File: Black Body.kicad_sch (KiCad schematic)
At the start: 20 parts, among them IC2 MCP96L00T-E_MX, J1 53307-2471, J2 Conn_01x02, J3 Conn_01x03, J4 Conn_02x08_Top_Bottom

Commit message: Revision
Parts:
- added TP1, TP2, TP3, TP4, TP5, TP6, TP7, TP8: TestPoint, Connector_PinHeader_2.54mm:PinHeader_1x01_P2.54mm_Vertical, symbol Connector:TestPoint
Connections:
- net +3V3: now also TP4.1
- net GND: now also TP5.1, TP6.1, TP7.1, TP8.1
- net at IC2.19 (SCL), J1.6 (I2C1_SCL), J3.1 (Pin_1): now also TP1.1
- net at IC2.20 (SDA), J1.4 (I2C1_SDA), J3.2 (Pin_2): now also TP2.1
- net at J1.9 (ADC1_IN7), J3.3 (Pin_3): now also TP3.1

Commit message: Updated Layout
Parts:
- removed D1, D2, D3, D4: 3V3, Diode_SMD:D_0603_1608Metric_Pad1.05x0.95mm_HandSolder, symbol Device:D
- removed J3: Conn_01x03, Connector_Molex:Molex_Nano-Fit_105313-xx03_1x03_P2.50mm_Horizontal, symbol Connector_Generic:Conn_01x03
- removed R4: 1M, Resistor_SMD:R_0603_1608Metric_Pad0.98x0.95mm_HandSolder, symbol Device:R_US
- removed R7, R8: 2M, Resistor_SMD:R_0603_1608Metric_Pad0.98x0.95mm_HandSolder, symbol Device:R_US
- removed TP7, TP8: TestPoint, Connector_PinHeader_2.54mm:PinHeader_1x01_P2.54mm_Vertical, symbol Connector:TestPoint
- added D1, D2, D3, D4, D5: LED, LED_SMD:LED_0603_1608Metric_Pad1.05x0.95mm_HandSolder, symbol Device:LED
- added J3: Conn_01x03_Pin, Connector_Molex:Molex_Nano-Fit_105313-xx03_1x03_P2.50mm_Horizontal, symbol Connector:Conn_01x03_Pin
- added J5: Conn_01x06, Connector_Molex:Molex_Nano-Fit_105313-xx06_1x06_P2.50mm_Horizontal, symbol Connector_Generic:Conn_01x06
- added R1: 10k, Resistor_SMD:R_0805_2012Metric, symbol Device:R_US
- added R10, R4, R7, R8, R9: R, Resistor_SMD:R_0603_1608Metric_Pad0.98x0.95mm_HandSolder, symbol Device:R
- added R2, R3: 1.5k, Resistor_SMD:R_0805_2012Metric, symbol Device:R_US
- added TP_TC_1, TP_TC_2, TP_TC_F_1, TP_TC_F_2: TestPoint, Connector_PinHeader_2.54mm:PinHeader_1x01_P2.54mm_Vertical, symbol Connector:TestPoint
- J4: footprint MX150:CONN_SD-75900-001_2X08_MOL -> Blackbody Footprint:CONN_SD-75900-001_2X08_MOL
- renumbered TP5 to GND1, TP6 to GND2, TP3 to INT1, TP1 to IS_SCL1, TP2 to IS_SDA1, TP4 to VCC1
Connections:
- net +3V3: now also C2.2, J5.3 (Pin_3), R1.1, R10.2, R2.1, R3.1, R4.2, R7.2, R8.2, R9.2; no longer C2.1, IC2.8 (GND_6)
- net GND: now also C2.1, IC2.8 (GND_6), J4.8 (Pin_8), J5.1 (Pin_1), J5.2 (Pin_2); no longer C2.2
- net at FB1.1, J2.1 (Pin_1): now also TP_TC_1.1
- net at C3.1, IC2.2 (VIN+), R6.1: now also TP_TC_F_2.1
- net at C3.2, IC2.4 (VIN-), R5.1: now also TP_TC_F_1.1
- net I2C1_SCL: now reaches IC2.19 (SCL), IS_SCL1.1, J1.6 (I2C1_SCL)
- net I2C1_SCL: now also D3.1 (K), J3.2 (Pin_2), J5.5 (Pin_5), R2.2
- net I2C1_SDA: now reaches IC2.20 (SDA), IS_SDA1.1, J1.4 (I2C1_SDA)
- net I2C1_SDA: now also J3.1 (Pin_1), J5.4 (Pin_4), R3.2
- net INT: now reaches INT1.1, J1.9 (ADC1_IN7)
- net INT: now also J3.3 (Pin_3), J5.6 (Pin_6), R1.2
- net at FB2.1, J2.2 (Pin_2): now also TP_TC_2.1
- net Alert_1: now reaches IC2.11 (ALERT_1)
- net Alert_1: now also J1.12 (SPI2_NSS)
- net Alert_2: now reaches IC2.12 (ALERT_2)
- net Alert_2: now also J1.18 (SPI2_SCK)
- net Alert_3: now reaches IC2.14 (ALERT_3)
- net Alert_3: now also J1.16 (SPI2_MOSI)
- net Alert_4: now reaches IC2.15 (ALERT_4)
- net Alert_4: now also J1.14 (SPI2_MISO)
- net DB_Conn_2: now reaches J1.17 (SPI1_MOSI)
- net DB_Conn_2: now also D4.1 (K)
- net Heartbeat: now reaches J1.19 (SPI1_NSS)
- net Heartbeat: now also D2.1 (K)
- net CAN_L: now reaches J1.20 (CAN_L), J4.6 (Pin_6)
- net CAN_L: now also J4.12 (Pin_12)
- net DB_Conn_3: now reaches J1.21 (SPI1_MISO)
- net DB_Conn_3: now also D5.1 (K)
- net CAN_H: now reaches J1.22 (CAN_H), J4.5 (Pin_5)
- net CAN_H: now also J4.13 (Pin_13)
- net DB_Conn_1: now reaches J1.23 (SPI1_SCK)
- net DB_Conn_1: now also D1.1 (K)
- net +24V: now reaches J1.24 (+24V_In), J4.1 (Pin_1)
- net +24V: now also J4.9 (Pin_9)
- new net: D1.2 (A), R4.1
- new net: D2.2 (A), R8.1
- new net: D4.2 (A), R7.1
- new net: D5.2 (A), R10.1
- new net: D3.2 (A), R9.1
- no-connect marks 34 -> 18
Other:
- moved on the sheet: C2, C3, FB1, FB2, GND1, GND2, IC2, INT1, IS_SCL1, IS_SDA1, J1, J2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

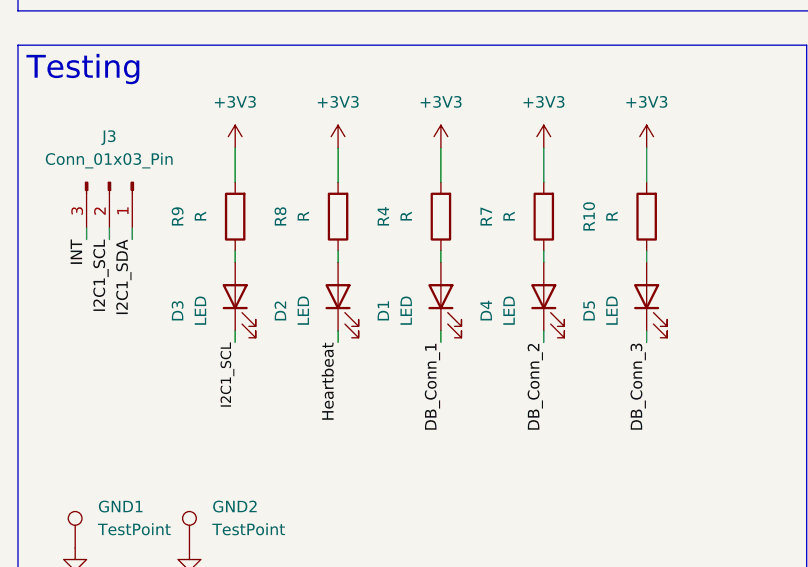
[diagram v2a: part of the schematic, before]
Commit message: resistors added
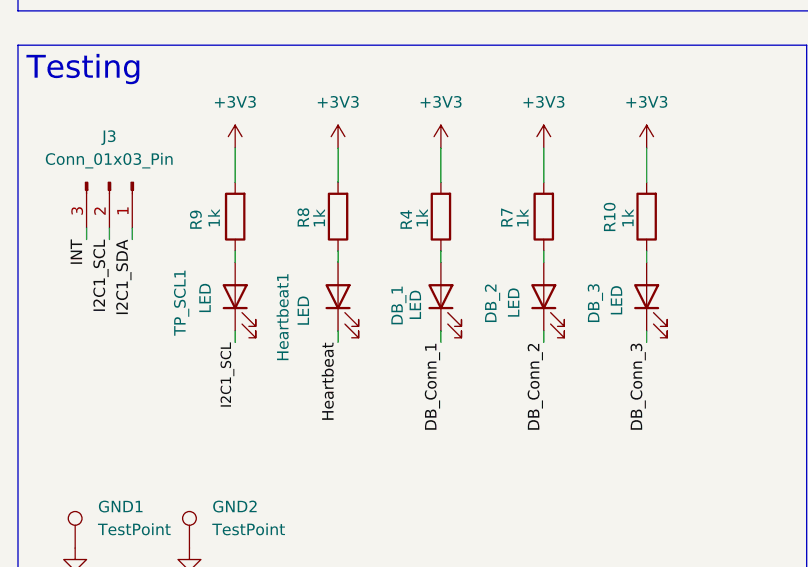
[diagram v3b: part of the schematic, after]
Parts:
- J4: footprint Blackbody Footprint:CONN_SD-75900-001_2X08_MOL -> UTSVT_Connectors:CONN_SD-75900-001_2X08_MOL
- R10, R4, R7, R8, R9: value R -> 1k
- renumbered D1 to DB_1, D4 to DB_2, D5 to DB_3, D2 to Heartbeat1, D3 to TP_SCL1
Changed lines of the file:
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@@
 		(on_board yes)
 		(dnp no)
-		(fields_autoplaced yes)
-		(property "Reference" "D1"
-			(at 57.15 138.7475 0)
+		(property "Reference" "DB_1"
+			(at 58.674 135.89 0)
 			(effects
 				(font
 					(size 1.27 1.27)
 				)
+				(justify right)
 			)
 		)
 		(property "Value" "LED"
-			(at 59.69 138.7475 0)
+			(at 60.706 136.398 0)
 			(effects
 				(font
 					(size 1.27 1.27)
 				)
+				(justify right)
 			)
 		)
@@
 			(project "Black Body"
 				(path "/326551d7-59c6-4bc5-b0df-e38f608d8925"
-					(reference "D1")
+					(reference "DB_1")
 					(unit 1)
 				)
@@
 		(on_board yes)
 		(dnp no)
-		(fields_autoplaced yes)
-		(property "Reference" "D2"
-			(at 45.72 138.7475 0)
+		(property "Reference" "Heartbeat1"
+			(at 45.974 139.446 0)
 			(effects
 				(font
@@
 			(project "Black Body"
 				(path "/326551d7-59c6-4bc5-b0df-e38f608d8925"
-					(reference "D2")
+					(reference "Heartbeat1")
 					(unit 1)
 				)
@@
 		(on_board yes)
 		(dnp no)
-		(fields_autoplaced yes)
 		(property "Reference" "R7"
-			(at 68.58 128.27 90)
+			(at 70.866 129.54 90)
 			(effects
 				(font
 					(size 1.27 1.27)
 				)
+				(justify right)
 			)
 		)
-		(property "Value" "R"
-			(at 71.12 128.27 90)
+		(property "Value" "1k"
+			(at 72.644 129.54 90)
 			(effects
 				(font
 					(size 1.27 1.27)
 				)
+				(justify right)
 			)
 		)
@@
 		(on_board yes)
 		(dnp no)
-		(fields_autoplaced yes)
-		(property "Reference" "D5"
-			(at 80.01 138.7475 0)
+		(property "Reference" "DB_3"
+			(at 80.518 135.636 0)
 			(effects
 				(font
 					(size 1.27 1.27)
 				)
+				(justify right)
 			)
 		)
 		(property "Value" "LED"
-			(at 82.55 138.7475 0)
+			(at 83.058 135.89 0)
 			(effects
 				(font
 					(size 1.27 1.27)
 				)
+				(justify right)
 			)
 		)
@@
 			(project "Black Body"
 				(path "/326551d7-59c6-4bc5-b0df-e38f608d8925"
-					(reference "D5")
+					(reference "DB_3")
 					(unit 1)
 				)
@@
 		(on_board yes)
 		(dnp no)
-		(fields_autoplaced yes)
 		(property "Reference" "R9"
-			(at 34.29 128.27 90)
+			(at 36.322 129.794 90)
 			(effects
 				(font
 					(size 1.27 1.27)
 				)
+				(justify right)
 			)
 		)
-		(property "Value" "R"
-			(at 36.83 128.27 90)
+		(property "Value" "1k"
+			(at 38.354 129.54 90)
 			(effects
 				(font
 					(size 1.27 1.27)
 				)
+				(justify right)
 			)
 		)
@@
 		(on_board yes)
 		(dnp no)
-		(fields_autoplaced yes)
-		(property "Reference" "D4"
-			(at 68.58 138.7475 0)
+		(property "Reference" "DB_2"
+			(at 69.088 135.636 0)
 			(effects
 				(font
 					(size 1.27 1.27)
 				)
+				(justify right)
 			)
 		)
 		(property "Value" "LED"
-			(at 71.12 138.7475 0)
+			(at 71.628 136.144 0)
 			(effects
 				(font
 					(size 1.27 1.27)
 				)
+				(justify right)
 			)
 		)
@@
 			(project "Black Body"
 				(path "/326551d7-59c6-4bc5-b0df-e38f608d8925"
-					(reference "D4")
+					(reference "DB_2")
 					(unit 1)
 				)
@@
 		(on_board yes)
 		(dnp no)
-		(fields_autoplaced yes)
 		(property "Reference" "R10"
-			(at 80.01 128.27 90)
+			(at 82.296 130.048 90)
 			(effects
 				(font
 					(size 1.27 1.27)
 				)
+				(justify right)
 			)
 		)
-		(property "Value" "R"
-			(at 82.55 128.27 90)
+		(property "Value" "1k"
+			(at 84.328 129.54 90)
 			(effects
 				(font
 					(size 1.27 1.27)
 				)
+				(justify right)
 			)
 		)
@@
 		(on_board yes)
 		(dnp no)
-		(fields_autoplaced yes)
 		(property "Reference" "R8"
-			(at 45.72 128.27 90)
+			(at 48.26 129.54 90)
 			(effects
 				(font
 					(size 1.27 1.27)
 				)
+				(justify right)
 			)
 		)
-		(property "Value" "R"
-			(at 48.26 128.27 90)
+		(property "Value" "1k"
+			(at 50.038 129.54 90)
 			(effects
 				(font
 					(size 1.27 1.27)
 				)
+				(justify right)
 			)
 		)
@@
 		(on_board yes)
 		(dnp no)
-		(fields_autoplaced yes)
 		(property "Reference" "R4"
-			(at 57.15 128.27 90)
+			(at 59.69 129.794 90)
 			(effects
 				(font
 					(size 1.27 1.27)
 				)
+				(justify right)
 			)
 		)
-		(property "Value" "R"
-			(at 59.69 128.27 90)
+		(property "Value" "1k"
+			(at 61.468 129.54 90)
 			(effects
 				(font
 					(size 1.27 1.27)
 				)
+				(justify right)
 			)
 		)
@@
 		(on_board yes)
 		(dnp no)
-		(fields_autoplaced yes)
-		(property "Reference" "D3"
-			(at 34.29 138.7475 0)
+		(property "Reference" "TP_SCL1"
+			(at 34.544 134.112 0)
 			(effects
 				(font
 					(size 1.27 1.27)
 				)
+				(justify right)
 			)
 		)
 		(property "Value" "LED"
-			(at 36.83 138.7475 0)
+			(at 37.338 135.636 0)
 			(effects
 				(font
 					(size 1.27 1.27)
 				)
+				(justify right)
 			)
 		)
@@
 			(project "Black Body"
 				(path "/326551d7-59c6-4bc5-b0df-e38f608d8925"
-					(reference "D3")
+					(reference "TP_SCL1")
 					(unit 1)
 				)
@@
 			)
 		)
-		(property "Footprint" "Blackbody Footprint:CONN_SD-75900-001_2X08_MOL"
+		(property "Footprint" "UTSVT_Connectors:CONN_SD-75900-001_2X08_MOL"
 			(at 135.89 132.08 0)
 			(effects

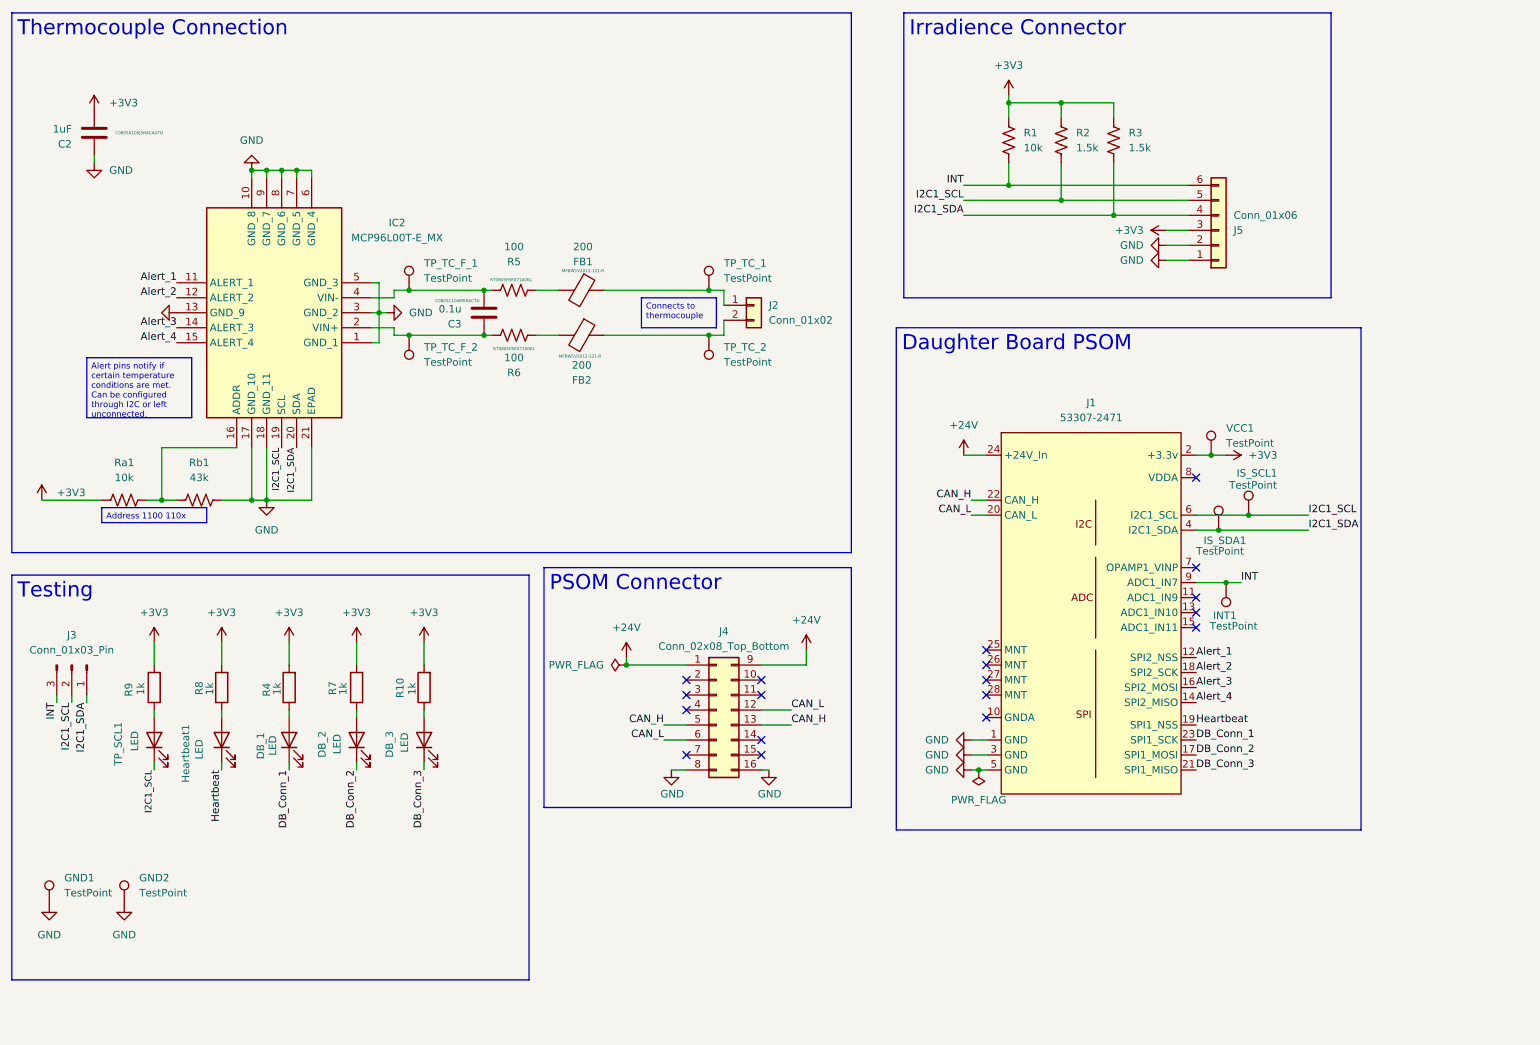
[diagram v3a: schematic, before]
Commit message: updated layout
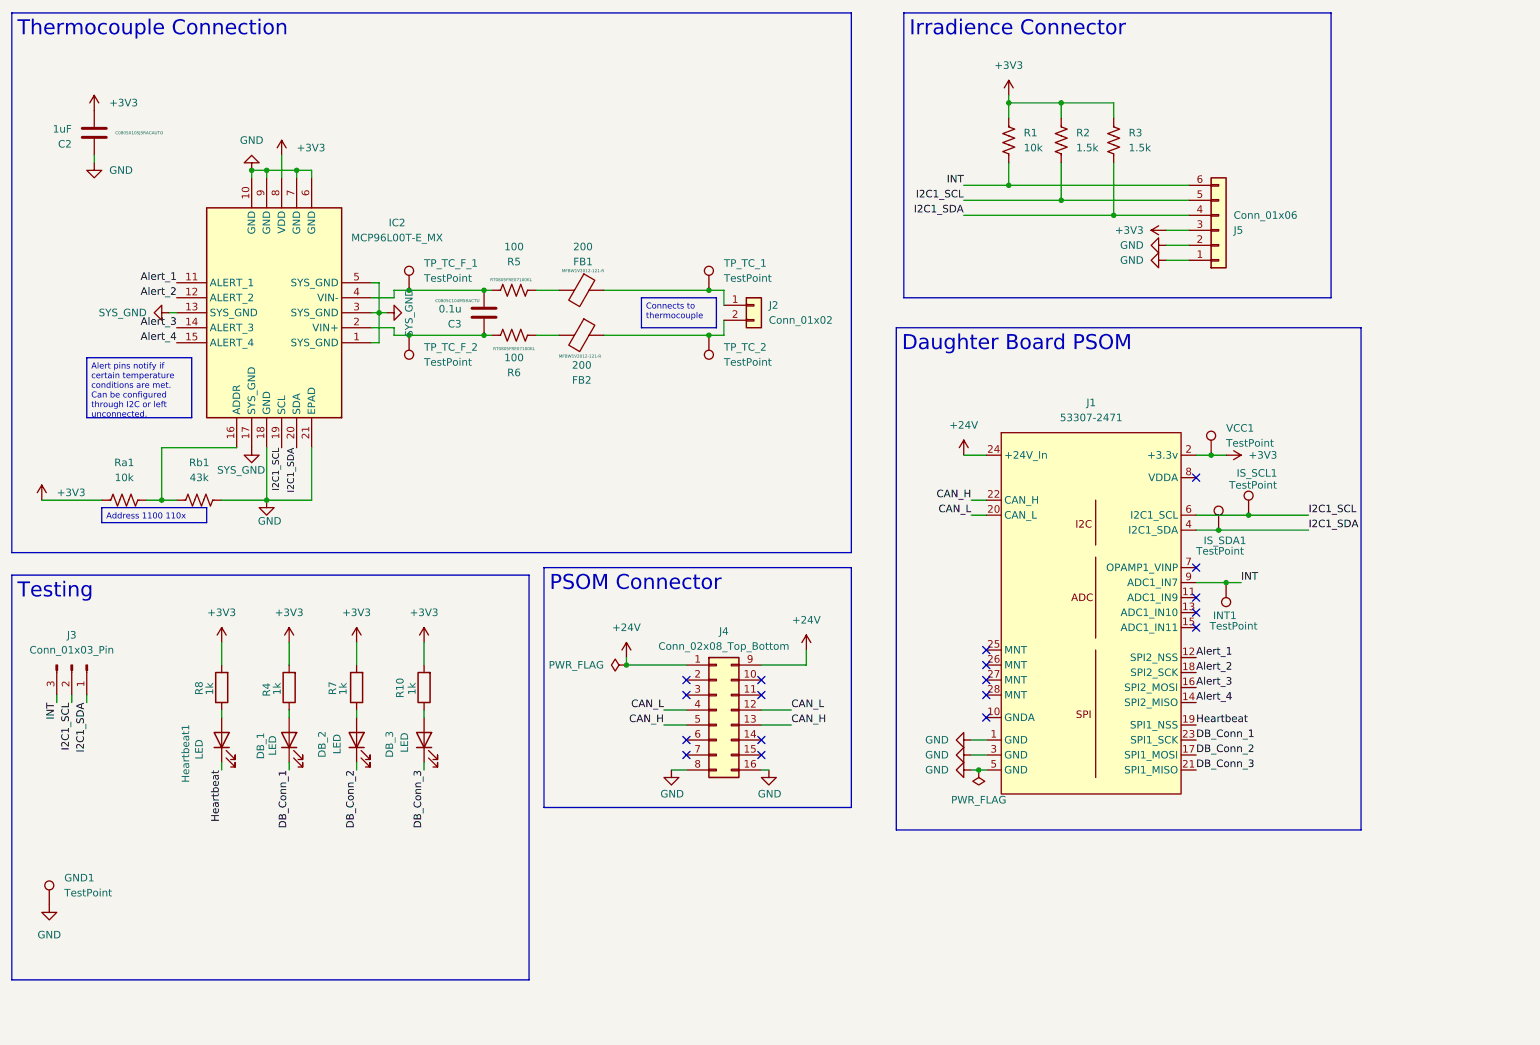
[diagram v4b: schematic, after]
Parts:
- removed GND2: TestPoint, Connector_PinHeader_2.54mm:PinHeader_1x01_P2.54mm_Vertical, symbol Connector:TestPoint
- removed R9: 1k, Resistor_SMD:R_0603_1608Metric_Pad0.98x0.95mm_HandSolder, symbol Device:R
- removed TP_SCL1: LED, LED_SMD:LED_0603_1608Metric_Pad1.05x0.95mm_HandSolder, symbol Device:LED
- IC2: footprint Blackbody Footprint:QFN65P500X500X100-21N-D -> QFN65P500X500X100-21N-D
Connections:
- net +3V3: now also IC2.8 (VDD)
- net CAN_L: now also J4.4 (Pin_4); no longer J4.6 (Pin_6)
- net GND: no longer IC2.1 (GND_1), IC2.13 (GND_9), IC2.17 (GND_10), IC2.3 (GND_2), IC2.5 (GND_3), IC2.8 (GND_6)
- new net SYS_GND: IC2.1 (SYS_GND), IC2.13 (SYS_GND), IC2.17 (SYS_GND), IC2.3 (SYS_GND), IC2.5 (SYS_GND)

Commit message: updated bb
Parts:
- removed J3: Conn_01x03_Pin, Connector_Molex:Molex_Nano-Fit_105313-xx03_1x03_P2.50mm_Horizontal, symbol Connector:Conn_01x03_Pin
- added F1: 0.5, Fuse:Fuse_0603_1608Metric_Pad1.05x0.95mm_HandSolder, symbol Device:Fuse
- added J3: Conn_01x04, Connector_PinHeader_2.54mm:PinHeader_1x04_P2.54mm_Horizontal, symbol Connector_Generic:Conn_01x04
- added R9: 0, Resistor_SMD:R_0603_1608Metric_Pad0.98x0.95mm_HandSolder, symbol Device:R_US
- GND1, TP_TC_1, TP_TC_2, TP_TC_F_1, TP_TC_F_2, VCC1: footprint Connector_PinHeader_2.54mm:PinHeader_1x01_P2.54mm_Vertical -> TestPoint:TestPoint_Pad_1.0x1.0mm
- IC2: footprint QFN65P500X500X100-21N-D -> Blackbody Footprint:QFN65P500X500X100-21N-D
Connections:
- net +24V: now also F1.2; no longer J4.9 (Pin_9)
- net GND: now also J3.4 (Pin_4), R9.2
- net I2C1_SCL: now also J3.2 (Pin_2)
- net I2C1_SDA: now also J3.3 (Pin_3)
- net INT: now also J3.1 (Pin_1)
- net SYS_GND: now also R9.1
- new net: F1.1, J4.9 (Pin_9)
